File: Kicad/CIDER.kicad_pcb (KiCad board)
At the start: 4 copper layers, 74.9 x 57.1 mm, 52 parts, among them CN1 CDTV-DIAG, J1 JTAG, J2 LED, J3 Conn_02x22_Odd_Even, SW1 SW_DIP_x04, U1 AZ1117-3.3, U10 SST39SF010, U2 XC95144XL-TQ100, U3 74HCT245, U4 74HCT245, U5 74HCT245, U6 74LVC245, U7 74LVC245, U8 MT48LC8M16A2P, U9 29F160, X1 50MHz

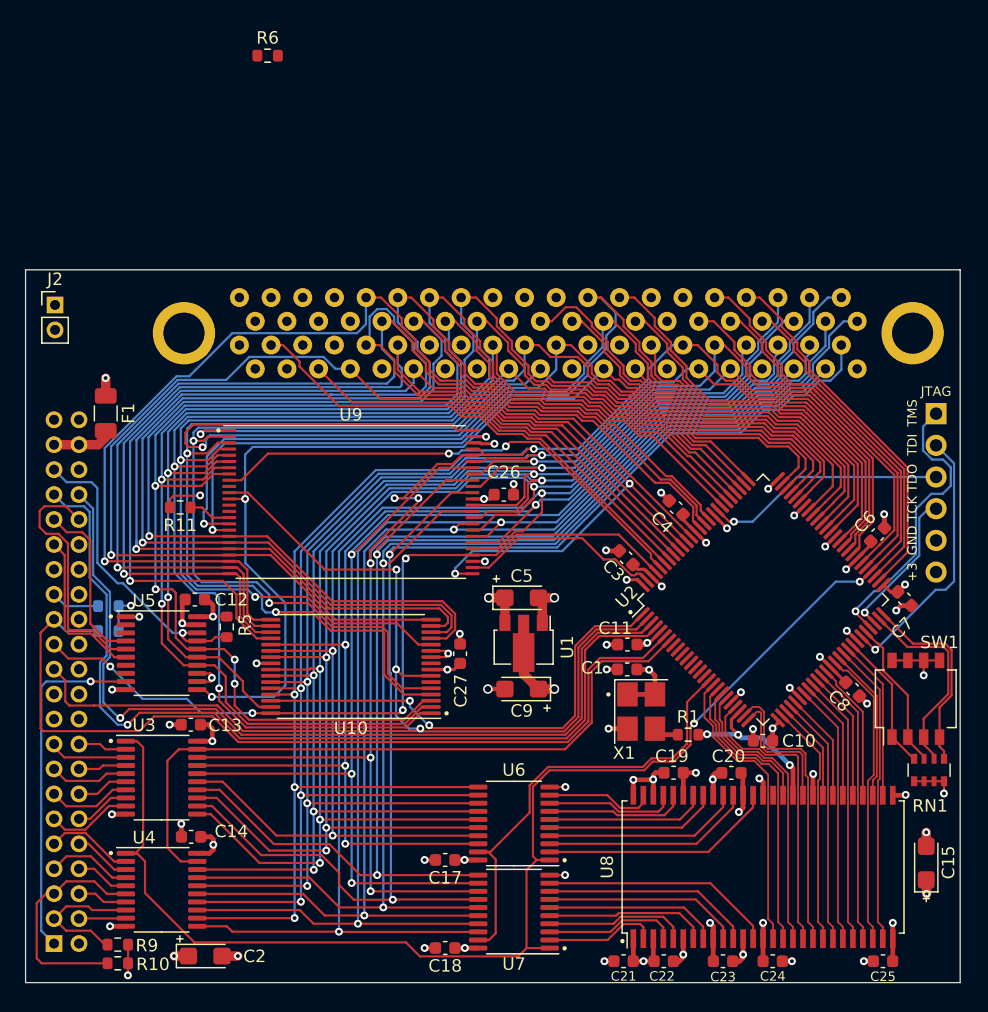
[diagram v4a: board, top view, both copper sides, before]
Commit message: PCB: Route Flash bank switch jumper
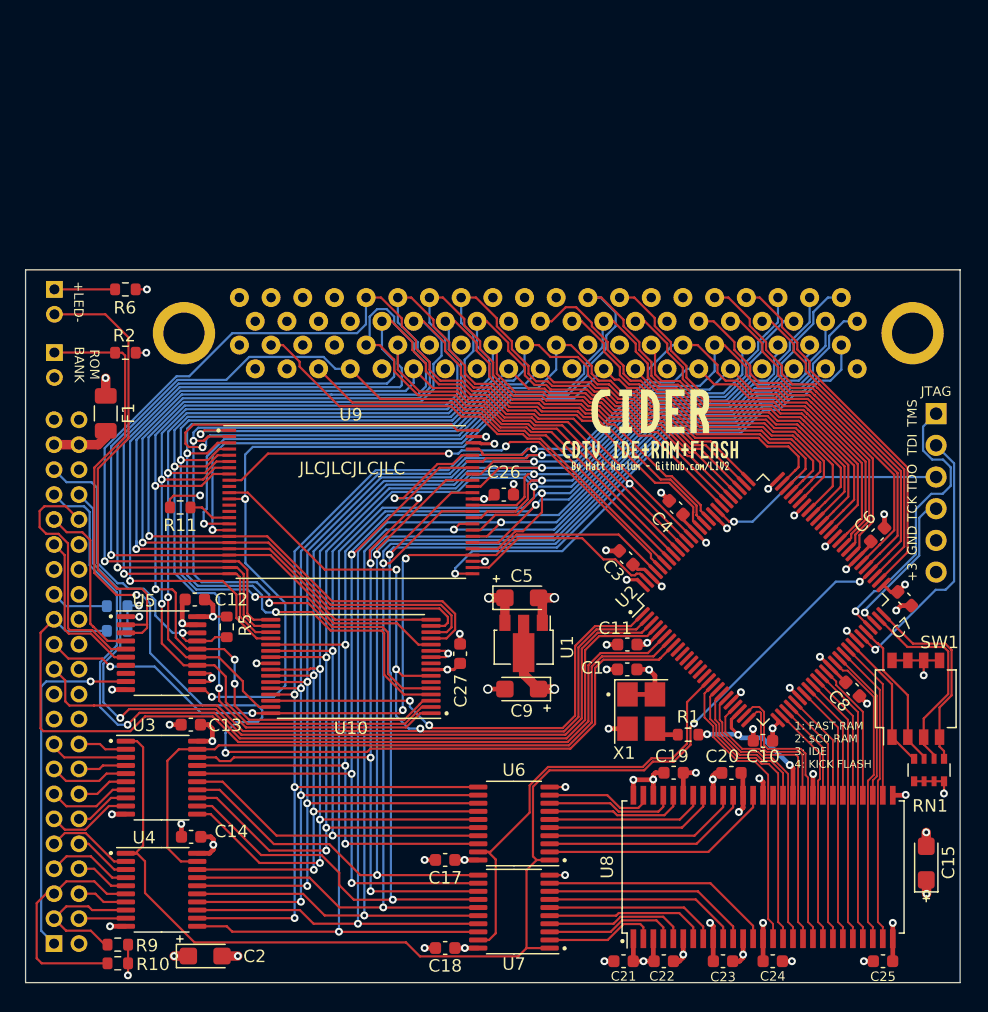
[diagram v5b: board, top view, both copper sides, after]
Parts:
- added J4: LED, Connector_PinHeader_2.00mm:PinHeader_1x02_P2.00mm_Vertical, B.Cu at (107.7, 100.6)
- added R2: 10K, Resistor_SMD:R_0603_1608Metric, F.Cu at (113.4, 100.6)
- added kibuzzard-63D81BD7: G***, kibuzzard-63D81BD7, F.Cu at (155.5, 105.3)
- added kibuzzard-63D81BF2: G***, kibuzzard-63D81BF2, F.Cu at (155.5, 108.4)
- added kibuzzard-63D81D74: G***, kibuzzard-63D81D74, F.Cu at (155.5, 109.7)
- J2: moved to B.Cu
- moved R6 21.9 mm to (113.4, 95.5), turned to 180 degrees
- moved J2 1.25 mm to (107.7, 95.5), turned to 180 degrees
- moved R7 0.70 mm to (112.8, 122.9)
- moved R8 0.70 mm to (112.8, 120.9)
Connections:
- U2 pad 8: unconnected-(U2-Pad8) -> /Amiga+CPLD/FLASH_BANK
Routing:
- net /Amiga+CPLD/FLASH_BANK: track 0.00 -> 92.3 mm, vias 0 -> 2
- net /IDE/~{LED}: track 0.00 -> 37.4 mm
- net Net-(J2-Pad1): track 0.00 -> 4.86 mm
- net /Amiga+CPLD/IORDY: track 70.5 -> 71.4 mm
- net VCC: track 30.6 -> 31.4 mm, vias 12 -> 13
- net /IDE/~{DMACK}: track 3.92 -> 4.63 mm
- net /IDE/~{IDE_ACT}: track 24.6 -> 25.3 mm
- net /Amiga+CPLD/~{IDE_CS2}: track 70.5 -> 71.2 mm
- net /Amiga+CPLD/~{IDE_CS1}: track 73.2 -> 73.9 mm
- net /Amiga+CPLD/TCK: track 12.2 -> 11.6 mm
- net /Amiga+CPLD/TDI: track 22.2 -> 21.6 mm
- net GND: track 76.0 -> 76.3 mm, vias 51 -> 52
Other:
- board text added: "+LED-"
- board text added: "1: FAST RAM 2: $C0 RAM 3: IDE 4: KICK FLASH"
- board text added: "JLCJLCJLCJLC"
- board text added: "PROTO A JAN 2023"
- board text added: "ROM BANK"

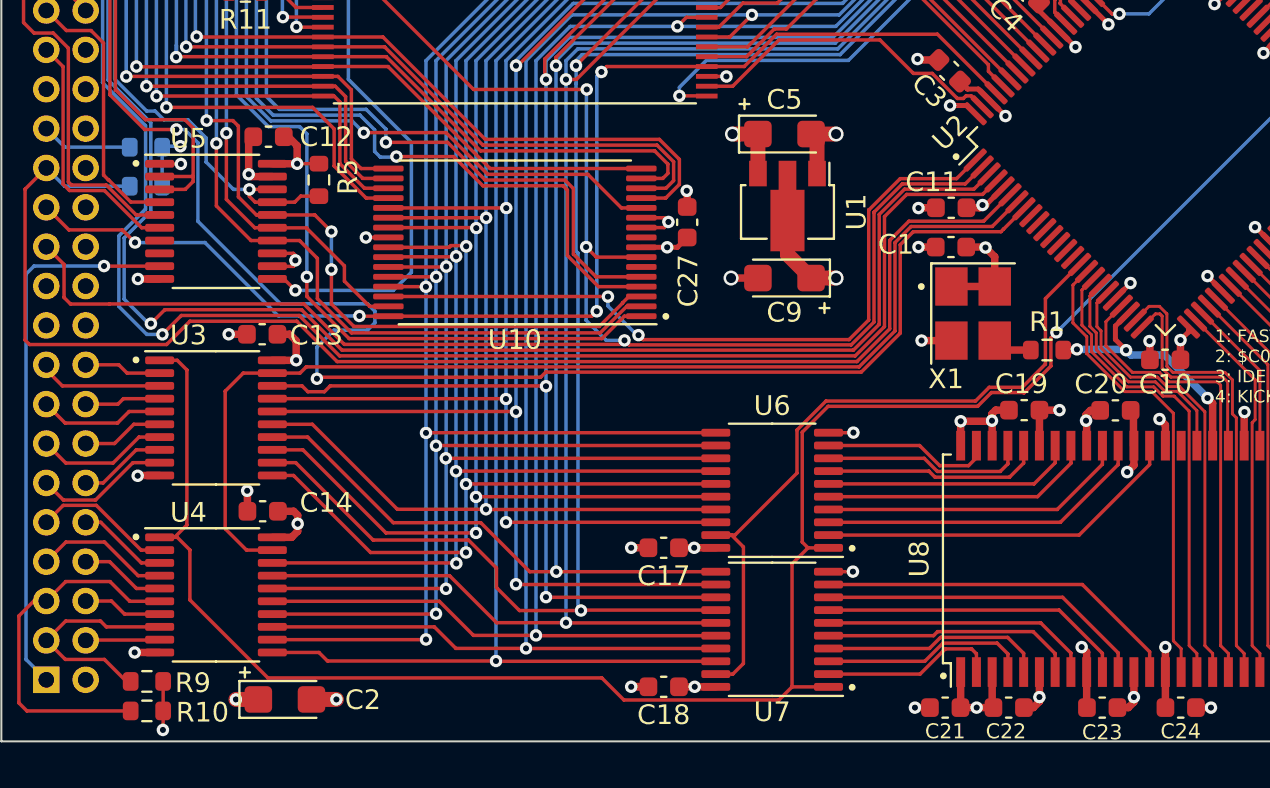
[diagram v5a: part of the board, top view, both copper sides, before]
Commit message: PCB: Add 22 Ohm series resistors for SDRAM
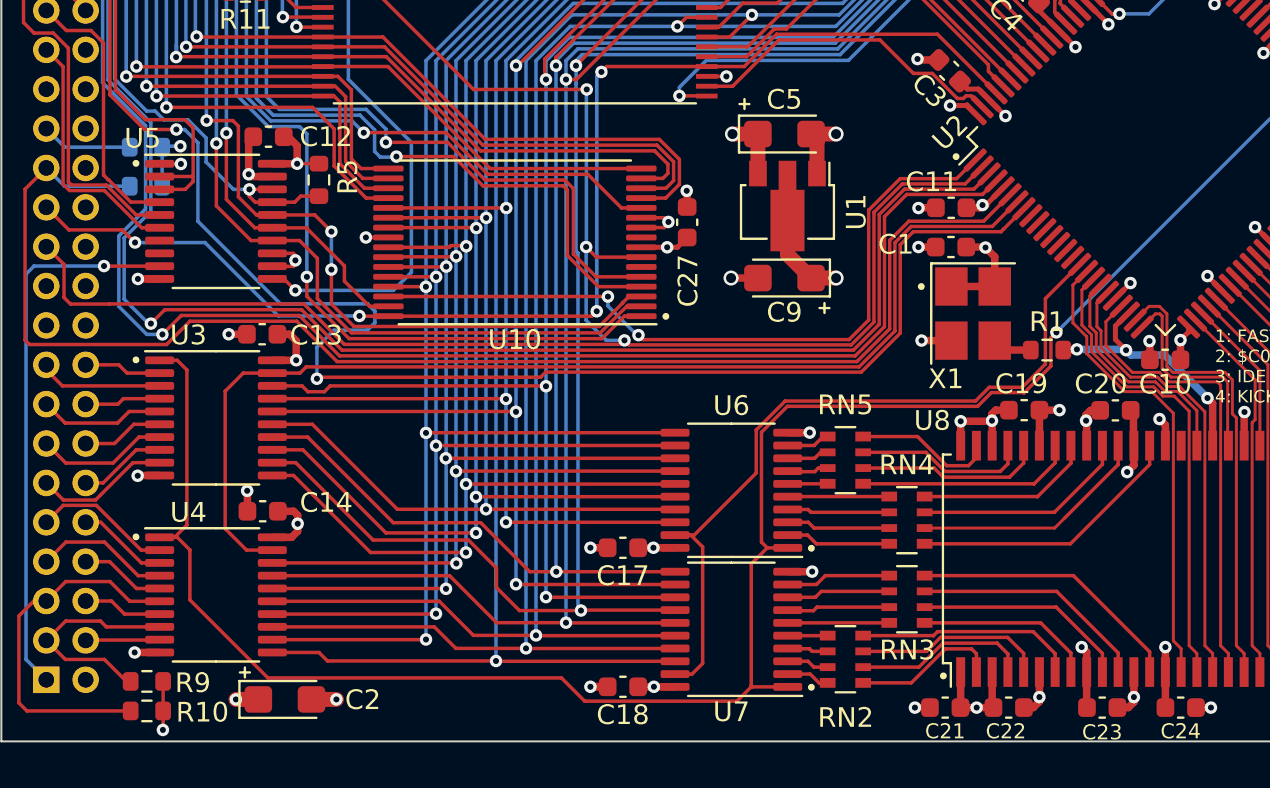
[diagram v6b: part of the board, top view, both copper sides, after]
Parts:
- added RN2: R_Pack04, Resistor_SMD:R_Array_Convex_4x0603, F.Cu at (148.3, 147.0)
- added RN3: R_Pack04, Resistor_SMD:R_Array_Convex_4x0603, F.Cu at (151.4, 143.9)
- added RN4: R_Pack04, Resistor_SMD:R_Array_Convex_4x0603, F.Cu at (151.4, 139.9)
- added RN5: R_Pack04, Resistor_SMD:R_Array_Convex_4x0603, F.Cu at (148.3, 136.8)
- C2, C5: value 10u -> 47u
- moved C17 2.07 mm to (137.0, 141.3)
- moved C18 2.07 mm to (137.0, 148.4)
- moved U6 2.07 mm to (142.5, 138.4)
- moved U7 2.07 mm to (142.5, 145.4)
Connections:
- U6 pad 2: /RAM/R_D8 -> Net-(RN4-Pad4)
- U6 pad 3: /RAM/R_D9 -> Net-(RN4-Pad3)
- U6 pad 4: /RAM/R_D10 -> Net-(RN4-Pad2)
- U6 pad 5: /RAM/R_D11 -> Net-(RN4-Pad1)
- U6 pad 6: /RAM/R_D12 -> Net-(RN5-Pad4)
- U6 pad 7: /RAM/R_D13 -> Net-(RN5-Pad3)
- U6 pad 8: /RAM/R_D14 -> Net-(U6-Pad8)
- U6 pad 9: /RAM/R_D15 -> Net-(U6-Pad9)
- U7 pad 2: /RAM/R_D0 -> Net-(U7-Pad2)
- U7 pad 3: /RAM/R_D1 -> Net-(U7-Pad3)
- U7 pad 4: /RAM/R_D2 -> Net-(U7-Pad4)
- U7 pad 5: /RAM/R_D3 -> Net-(U7-Pad5)
- U7 pad 6: /RAM/R_D4 -> Net-(U7-Pad6)
- U7 pad 7: /RAM/R_D5 -> Net-(U7-Pad7)
- U7 pad 8: /RAM/R_D6 -> Net-(U7-Pad8)
- U7 pad 9: /RAM/R_D7 -> Net-(U7-Pad9)
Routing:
- net Net-(U7-Pad9): track 0.00 -> 5.34 mm
- net Net-(RN4-Pad4): track 0.00 -> 5.34 mm
- net Net-(U7-Pad8): track 0.00 -> 5.28 mm
- net Net-(RN4-Pad3): track 0.00 -> 5.28 mm
- net Net-(RN4-Pad2): track 0.00 -> 5.21 mm
- net Net-(U7-Pad7): track 0.00 -> 5.20 mm
- net Net-(U7-Pad6): track 0.00 -> 5.15 mm
- net Net-(RN4-Pad1): track 0.00 -> 5.15 mm
- net /RAM/R_D4: track 13.9 -> 9.03 mm
- net /RAM/R_D11: track 13.4 -> 8.50 mm
- net /RAM/R_D10: track 15.8 -> 11.0 mm
- net /RAM/R_D5: track 15.8 -> 11.0 mm
- net /RAM/R_D9: track 16.9 -> 12.1 mm
- net /RAM/R_D6: track 16.9 -> 12.1 mm
- net /RAM/R_D8: track 18.8 -> 14.1 mm
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
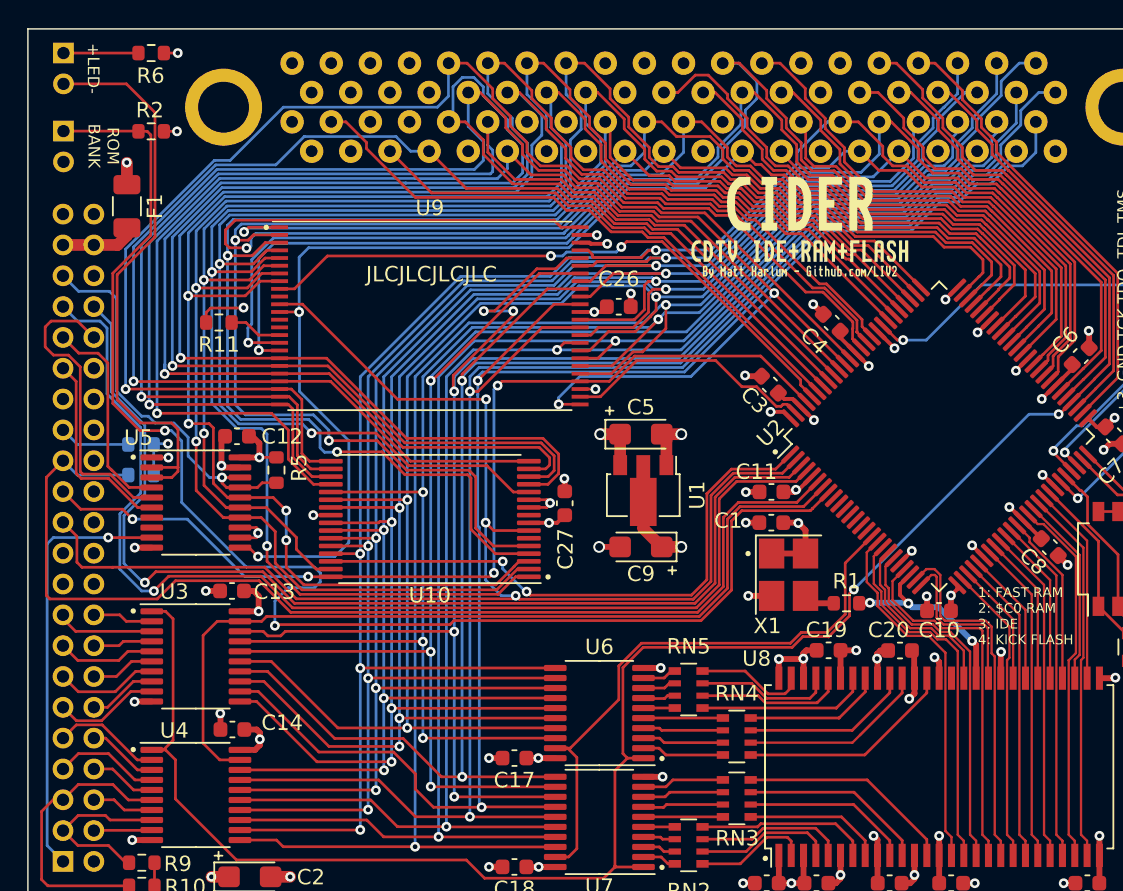
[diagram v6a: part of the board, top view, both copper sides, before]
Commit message: PCB: Connect Flash A18 to CPLD
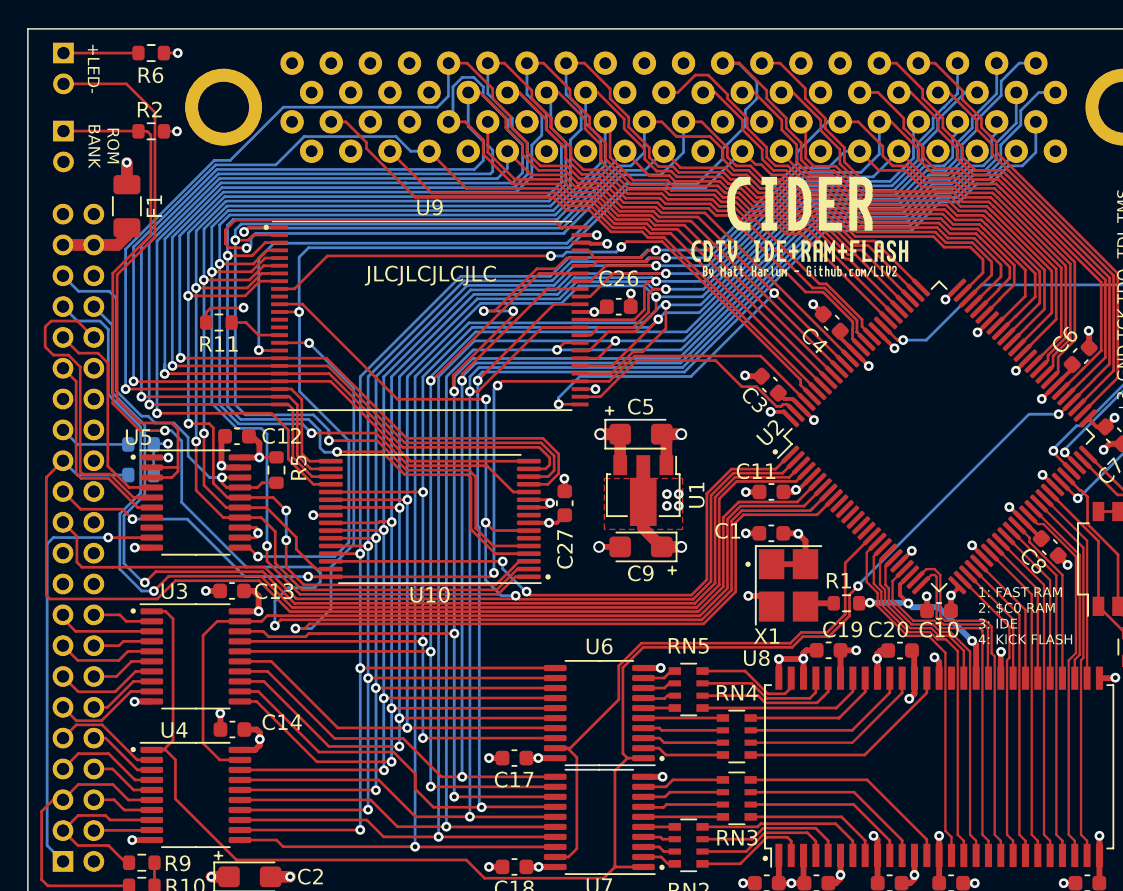
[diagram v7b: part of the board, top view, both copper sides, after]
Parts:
- moved C1 0.69 mm to (153.6, 126.7)
- moved X1 0.69 mm to (154.8, 130.1)
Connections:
- U2 pad 9: unconnected-(U2-Pad9) -> /Amiga+CPLD/FLASH_A18
- U9 pad 16: /Amiga+CPLD/A19 -> /Amiga+CPLD/FLASH_A18
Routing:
- net /Amiga+CPLD/FLASH_A18: track 0.00 -> 64.9 mm, vias 0 -> 2
- net /Amiga+CPLD/A19: track 74.8 -> 29.6 mm, vias 1 -> 0
- net +3.3V: track 58.6 -> 58.5 mm, vias 19 -> 23
- added copper zone on F.Cu, net +3.3V

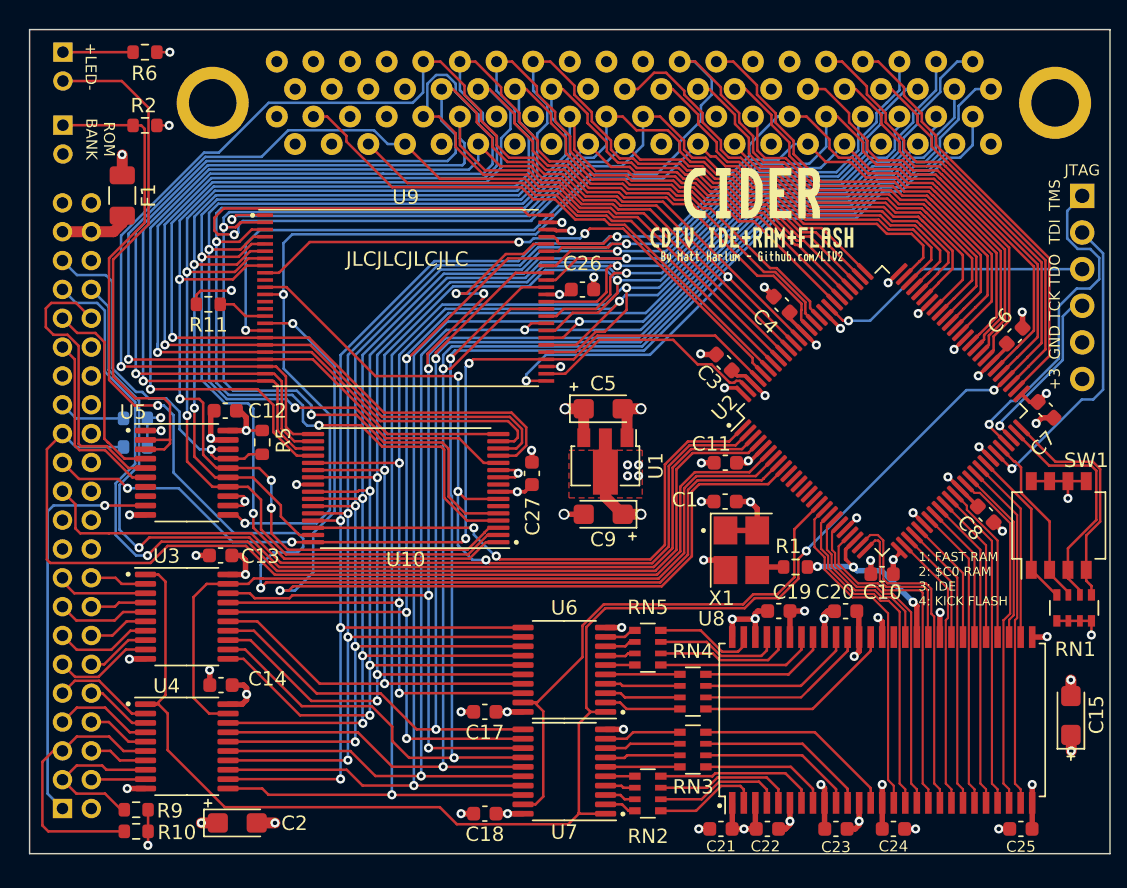
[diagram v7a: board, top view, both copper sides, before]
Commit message: PCB: Remove useless cfgin connection
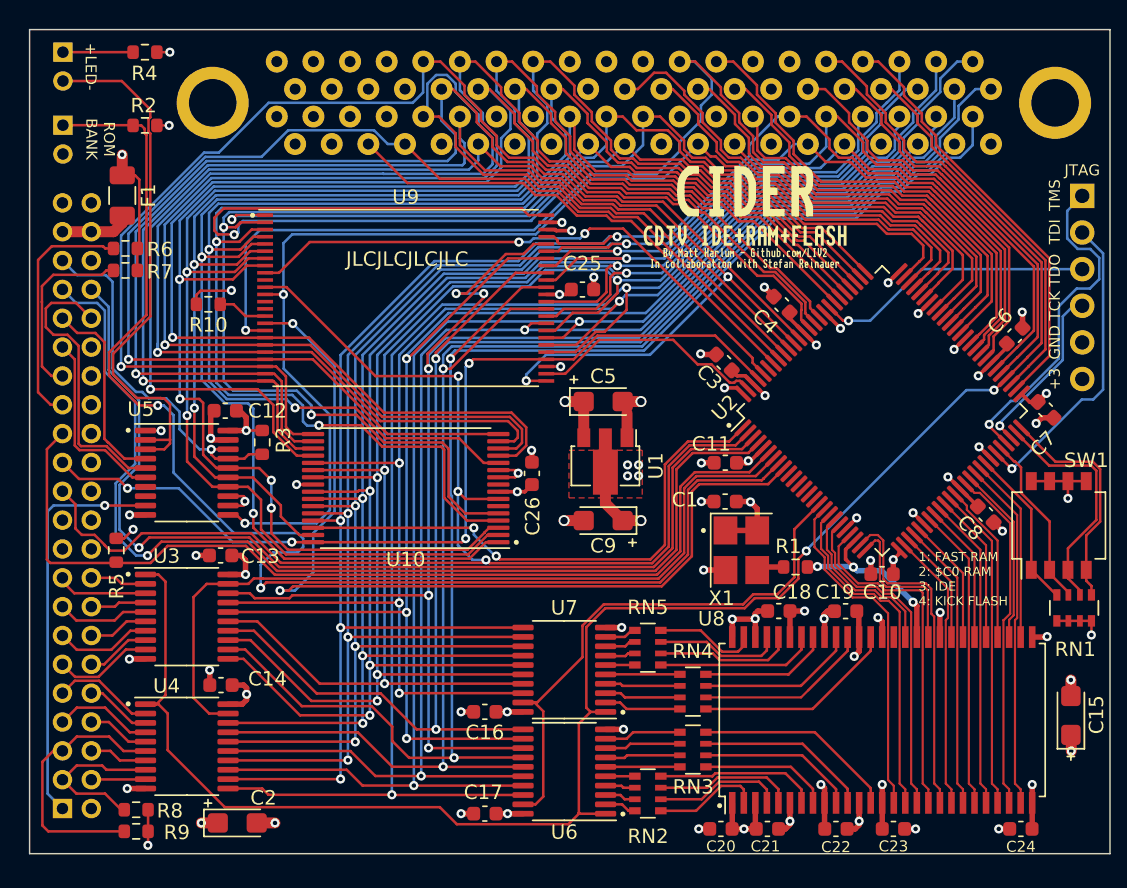
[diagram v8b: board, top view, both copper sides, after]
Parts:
- removed the R8 at (112.8, 120.9)
- removed kibuzzard-63D81D74: G***, kibuzzard-63D81D74
- added R6: 10K, Resistor_SMD:R_0603_1608Metric, F.Cu at (112.1, 109.2)
- added R7: 10K, Resistor_SMD:R_0603_1608Metric, F.Cu at (112.1, 110.7)
- added kibuzzard-63DCBD83: G***, kibuzzard-63DCBD83, F.Cu at (155.0, 110.2)
- added kibuzzard-63DCBE23: G***, kibuzzard-63DCBE23, F.Cu at (155.0, 109.5)
- R5: renamed from R7; moved to F.Cu
- moved R5 7.28 mm to (111.4, 130.1), turned to 90 degrees
- moved C5 0.50 mm to (145.2, 119.8)
- moved kibuzzard-63D81BD7 0.48 mm to (155.0, 105.2)
- moved kibuzzard-63D81BF2 0.48 mm to (155.0, 108.3)
- moved C9 0.44 mm to (145.2, 128.0)
- renumbered C17 to C16, C18 to C17, C19 to C18, C20 to C19, C21 to C20, C22 to C21, C23 to C22, C24 to C23, C25 to C24, C26 to C25, C27 to C26, J4 to J2, J2 to J3, J3 to J4, R11 to R10, R5 to R3, R6 to R4, R9 to R8, R10 to R9, U7 to U6, U6 to U7
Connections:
- CN1 pad 5: /Amiga+CPLD/~{CFGIN} -> unconnected-(CN1-Pad5)
- J4 pad 44: unconnected-(J3-Pad44) -> GND
- U2 pad 95: /Amiga+CPLD/~{CFGIN} -> unconnected-(U2-Pad95)
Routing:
- net /Amiga+CPLD/~{CFGIN}: track 39.0 -> 0.00 mm
- net /IDE/~{IDE_IRQ}: track 0.00 -> 12.7 mm
- net /IDE/~{DMACK}: track 4.63 -> 16.9 mm
- net VCC: track 31.4 -> 37.6 mm
- net /Amiga+CPLD/IORDY: track 71.4 -> 66.8 mm
- net /Amiga+CPLD/~{IOWR}: track 90.9 -> 91.9 mm
